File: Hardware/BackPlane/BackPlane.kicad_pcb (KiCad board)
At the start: 2 copper layers, 100 x 96 mm, 5 parts

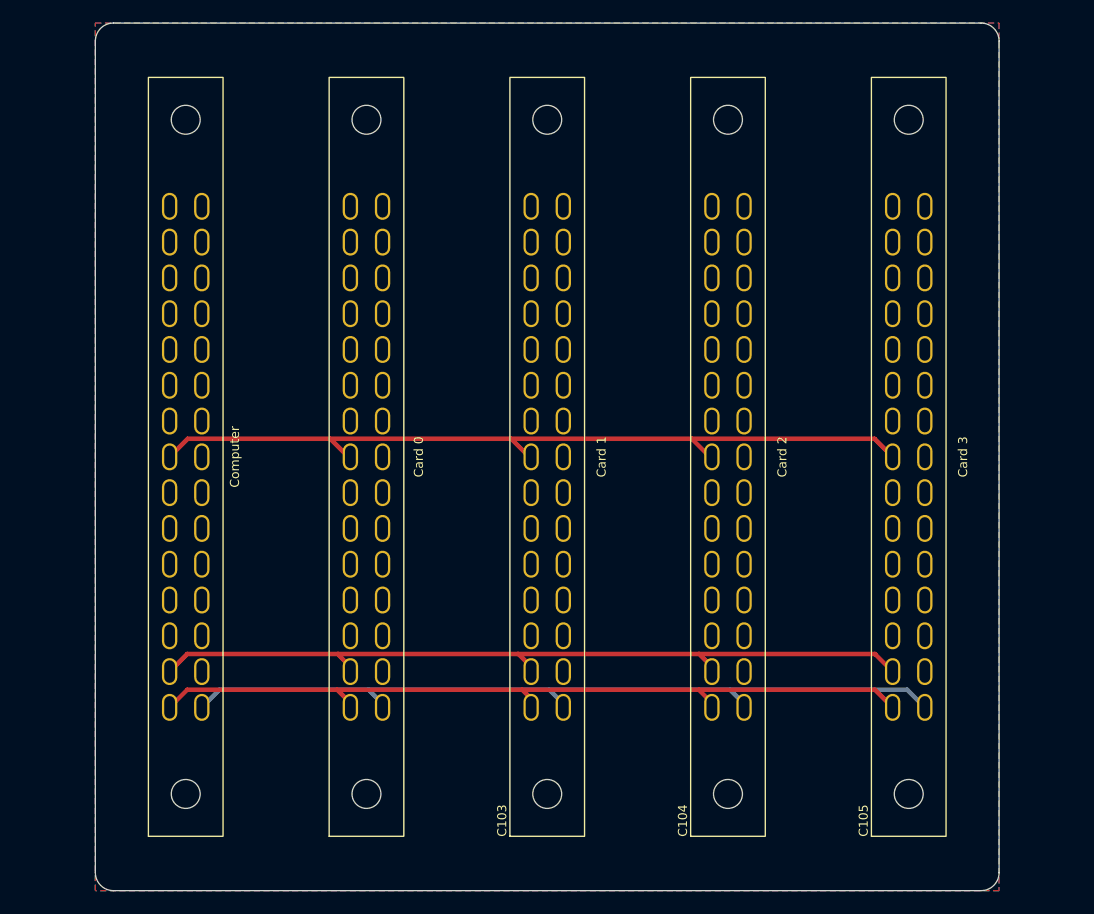
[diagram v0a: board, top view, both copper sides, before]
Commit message: Add body for backplane
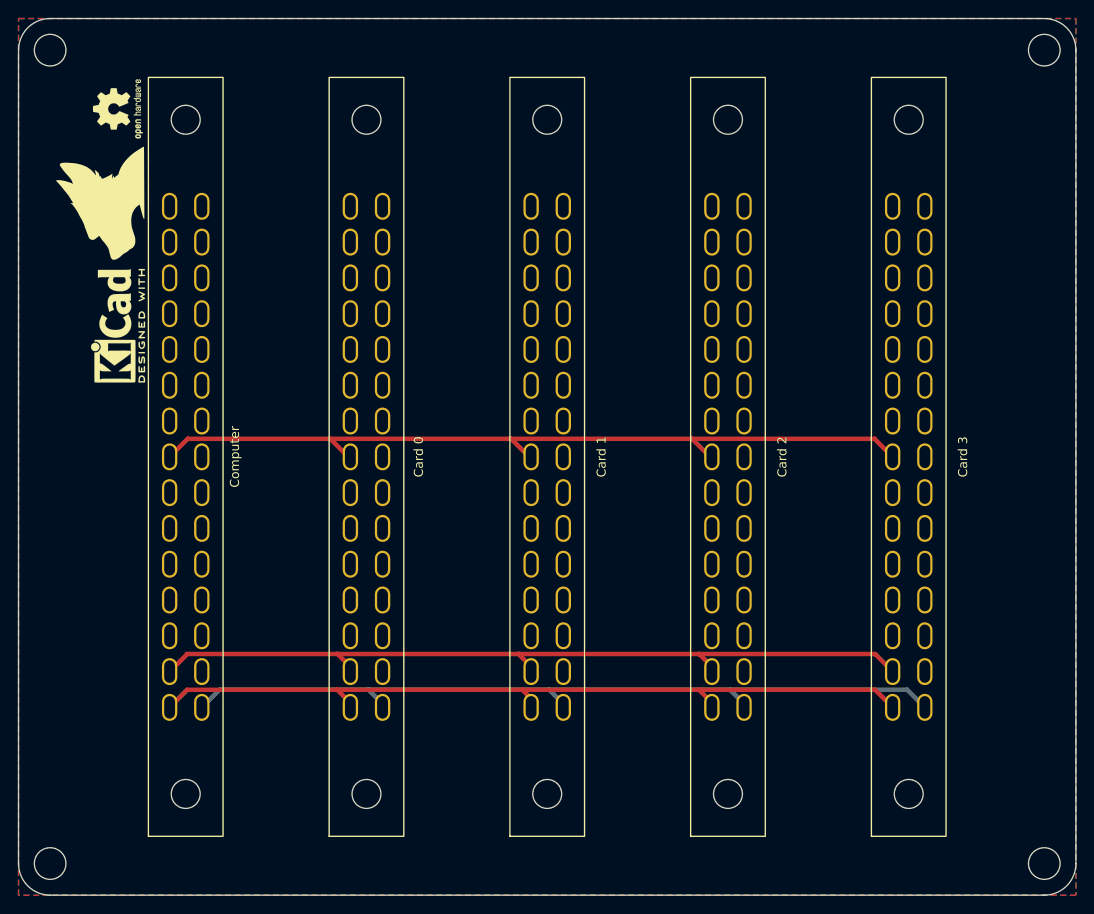
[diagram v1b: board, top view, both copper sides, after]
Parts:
- added G***: LOGO, KenwoodFox:KITSUNE_LOGO, F.Cu at (90.5, 72.0)
- added H101: MountingHole, MountingHole:MountingHole_3.5mm, F.Cu at (85.0, 55.0)
- added H102: MountingHole, MountingHole:MountingHole_3.5mm, F.Cu at (85.0, 145.0)
- added H103: MountingHole, MountingHole:MountingHole_3.5mm, F.Cu at (195.0, 55.0)
- added H104: MountingHole, MountingHole:MountingHole_3.5mm, F.Cu at (195.0, 145.0)
- added REF**: KiCad-Logo2_5mm_SilkScreen, Symbol:KiCad-Logo2_5mm_SilkScreen, F.Cu at (92.5, 85.5)
- added REF**: OSHW-Logo2_7.3x6mm_SilkScreen, Symbol:OSHW-Logo2_7.3x6mm_SilkScreen, F.Cu at (92.5, 61.5)
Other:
- board size 100 x 96 mm -> 117 x 97 mm

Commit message: Bump backplane
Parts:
- added J103: Power Harness, Connector_JST:JST_EH_B5B-EH-A_1x05_P2.50mm_Vertical, B.Cu at (91.5, 105.0)
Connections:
- C101 pad 1: +5V -> +12V
- C101 pad 11: unconnected-(C101-Pad11) -> /CARD_EN_0
- C101 pad 12: unconnected-(C101-Pad12) -> /CARD_EN_1
- C101 pad 13: unconnected-(C101-Pad13) -> /CARD_EN_2
- C101 pad 14: unconnected-(C101-Pad14) -> /CARD_EN_3
- C101 pad 16: +12V -> +5V
- C101 pad 26: unconnected-(C101-Pad26) -> /CARD_SEL_0
- C101 pad 27: unconnected-(C101-Pad27) -> /CARD_SEL_1
- C101 pad 28: unconnected-(C101-Pad28) -> /CARD_SEL_2
- C101 pad 29: unconnected-(C101-Pad29) -> /CARD_SEL_3
- C102 pad 1: +5V -> +12V
- C102 pad 14: unconnected-(C102-Pad14) -> /CARD_EN_0
- C102 pad 16: +12V -> +5V
- C102 pad 29: unconnected-(C102-Pad29) -> /CARD_SEL_0
- C103 pad 1: +5V -> +12V
- C103 pad 14: unconnected-(C103-Pad14) -> /CARD_EN_1
- C103 pad 16: +12V -> +5V
- C103 pad 29: unconnected-(C103-Pad29) -> /CARD_SEL_1
- C104 pad 1: +5V -> +12V
- C104 pad 14: unconnected-(C104-Pad14) -> /CARD_EN_2
- C104 pad 16: +12V -> +5V
- C104 pad 29: unconnected-(C104-Pad29) -> /CARD_SEL_2
- C105 pad 1: +5V -> +12V
- C105 pad 14: unconnected-(C105-Pad14) -> /CARD_EN_3
- C105 pad 16: +12V -> +5V
- C105 pad 29: unconnected-(C105-Pad29) -> /CARD_SEL_3
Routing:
- net /CARD_SEL_3: track 0.00 -> 81.6 mm
- net /CARD_EN_3: track 0.00 -> 81.6 mm
- net /CARD_SEL_2: track 0.00 -> 66.8 mm
- net +12V: track 90.8 -> 157.2 mm
- net /CARD_EN_2: track 0.00 -> 58.1 mm
- net /CARD_EN_1: track 0.00 -> 43.3 mm
- net /CARD_SEL_1: track 0.00 -> 41.6 mm
- net /CARD_SEL_0: track 0.00 -> 26.8 mm
- net /CARD_EN_0: track 0.00 -> 18.1 mm
- net +5V: track 89.4 -> 97.5 mm
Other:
- board text added: "12v"
- board text added: "5v"
- board text added: "GND"

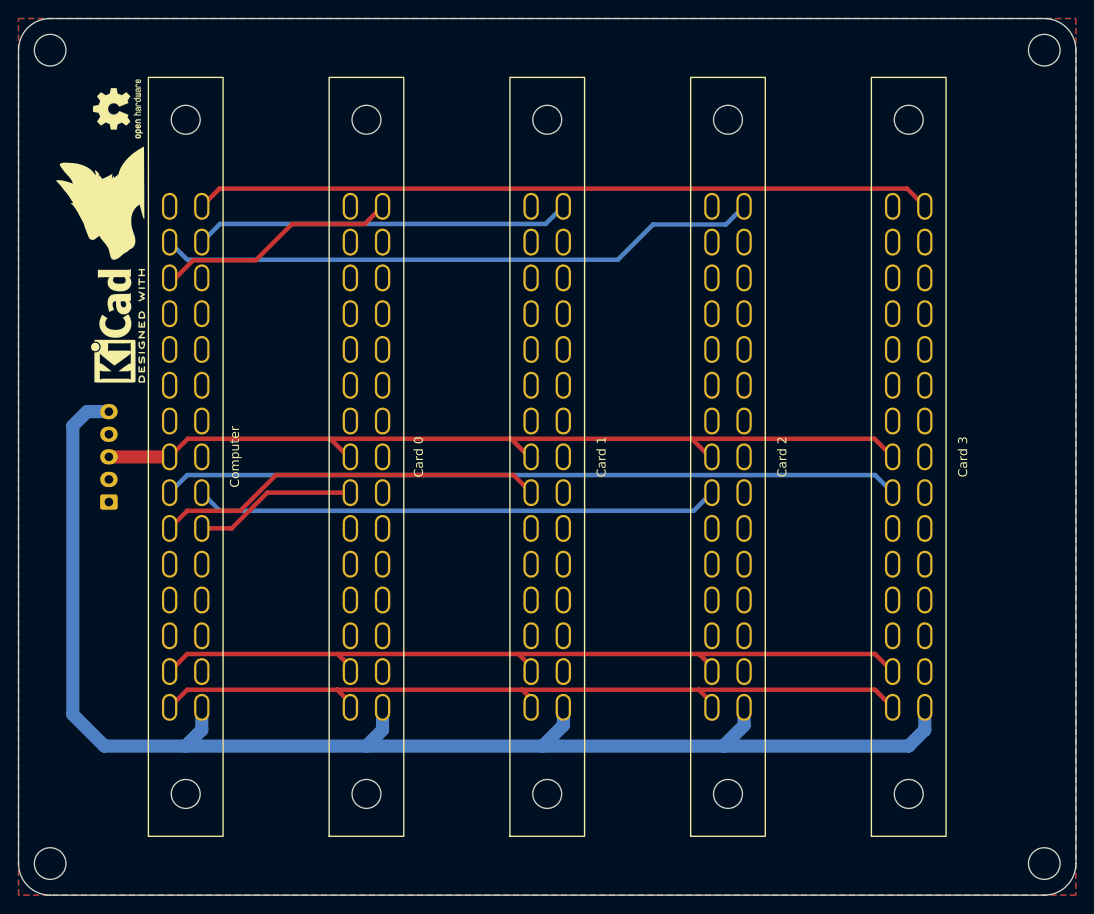
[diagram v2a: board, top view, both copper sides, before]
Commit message: Bump everything with new backplane design
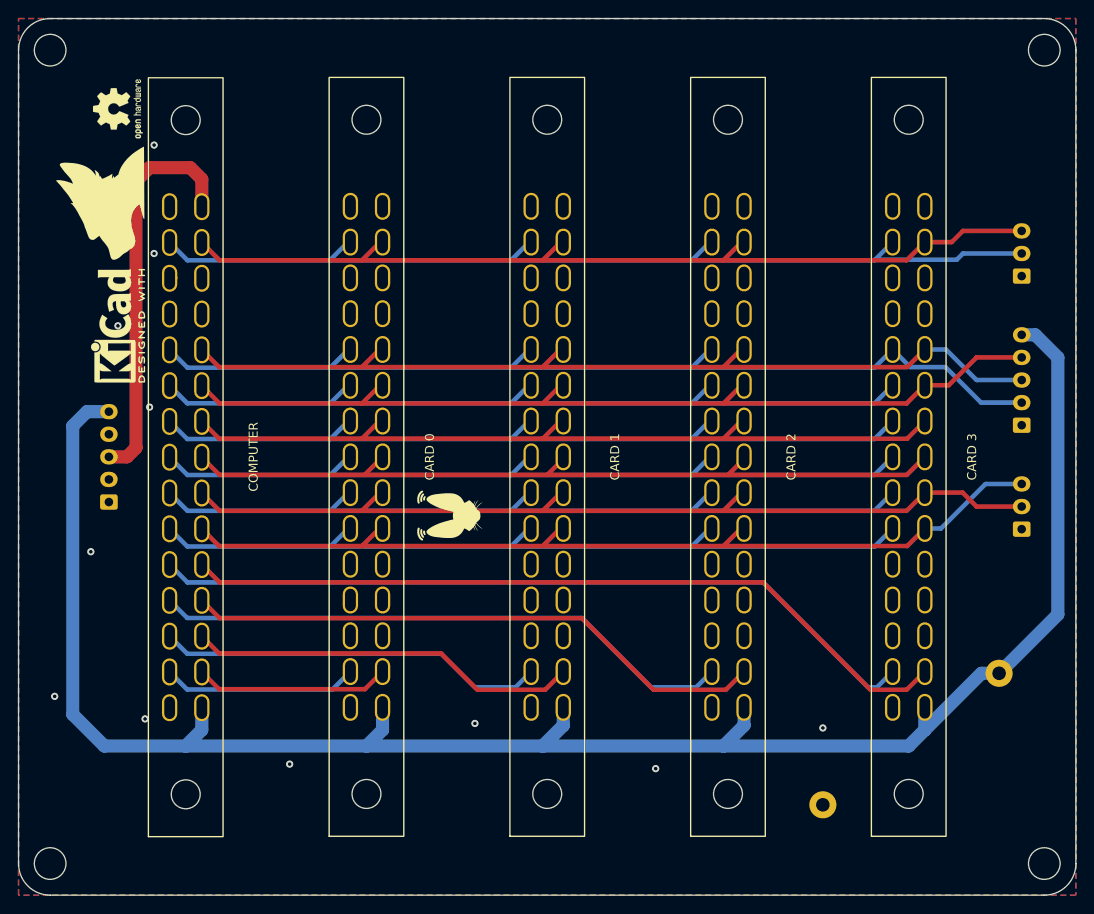
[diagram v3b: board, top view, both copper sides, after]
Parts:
- removed C101: Computer, KenwoodFox:EBM15DSEH
- removed C102: Card 0, KenwoodFox:EBM15DSEH
- removed C103: Card 1, KenwoodFox:EBM15DSEH
- removed C104: Card 2, KenwoodFox:EBM15DSEH
- removed C105: Card 3, KenwoodFox:EBM15DSEH
- added G***: LOGO, KenwoodFox:fennec_logo_solid_small, F.Cu at (129.0, 106.5)
- added J101: CAN, Connector_JST:JST_EH_B3B-EH-A_1x03_P2.50mm_Vertical, B.Cu at (192.5, 80.0)
- added J102: i²c, Connector_JST:JST_EH_B3B-EH-A_1x03_P2.50mm_Vertical, B.Cu at (192.5, 108.0)
- added J104: GPIO, Connector_JST:JST_EH_B5B-EH-A_1x05_P2.50mm_Vertical, B.Cu at (192.5, 96.5)
- added TP101: TestPoint, TestPoint:TestPoint_Loop_D2.54mm_Drill1.5mm_Beaded, B.Cu at (190.0, 124.0)
- added TP102: TestPoint, TestPoint:TestPoint_Loop_D2.54mm_Drill1.5mm_Beaded, B.Cu at (170.5, 138.5)
- added U101: COMPUTER, KenwoodFox:EBM15DSEH, F.Cu at (100.0, 100.0)
- added U102: CARD 0, KenwoodFox:EBM15DSEH, F.Cu at (120.0, 100.0)
- added U103: CARD 1, KenwoodFox:EBM15DSEH, F.Cu at (140.0, 100.0)
- added U104: CARD 2, KenwoodFox:EBM15DSEH, F.Cu at (160.0, 100.0)
- added U105: CARD 3, KenwoodFox:EBM15DSEH, F.Cu at (180.0, 100.0)
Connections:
- J103 pad 5: +12V -> Net-(J103-Pin_5)
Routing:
- net /GPIO3: track 0.00 -> 107.5 mm
- net /CANL: track 0.00 -> 107.3 mm
- net /GPIO1: track 0.00 -> 103.0 mm
- net /GPIO2: track 0.00 -> 103.0 mm
- net /CANH: track 0.00 -> 102.2 mm
- net GND: track 0.00 -> 92.0 mm, vias 0 -> 11
- net /SPI_SDO: track 0.00 -> 90.9 mm
- net /SPI_SDA2: track 0.00 -> 90.8 mm
- net /SPI_SDA1: track 0.00 -> 90.8 mm
- net /SPI_SDA3: track 0.00 -> 90.8 mm
- net /SPI_CLK: track 0.00 -> 90.8 mm
- net /SPI_SDA4: track 0.00 -> 90.8 mm
- net +12V: track 157.2 -> 210.7 mm
- net +5V: track 97.5 -> 44.4 mm
- net /I2C_CLK: track 89.1 -> 103.6 mm
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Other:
- board text added: "+12v"
- board text added: "12V"
- board text added: "CANH"
- board text added: "CANL"
- board text added: "GPIO1"
- board text added: "GPIO2"
- board text added: "GPIO3"
- board text added: "SCL"
- board text added: "SDA"
